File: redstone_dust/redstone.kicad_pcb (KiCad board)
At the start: 2 copper layers, 40 x 40 mm, 76 parts, among them J1 1x4_Pogo, J2 1x4_Pogo, J3 1x4_Pogo, J4 1x4_Pogo, J5 1x4_Pogo, J6 1x4_Pogo, J7 1x4_Pogo, J8 1x4_Pogo, J9 2.54mm_ProgrammingPin, Q1 BC108, Q2 BC108, Q3 BC108, Q4 BC108, SW1 SW_Push_Open, U1 RP2040, U3 TPS62162DSG

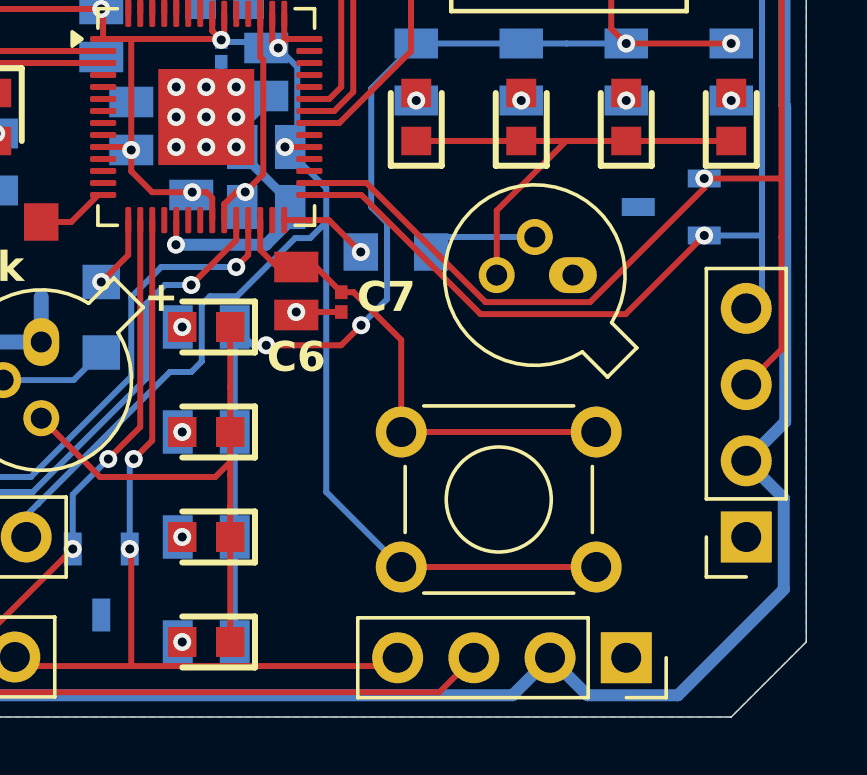
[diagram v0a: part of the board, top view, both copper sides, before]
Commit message: add dip switch to schematic, todo update pcb design
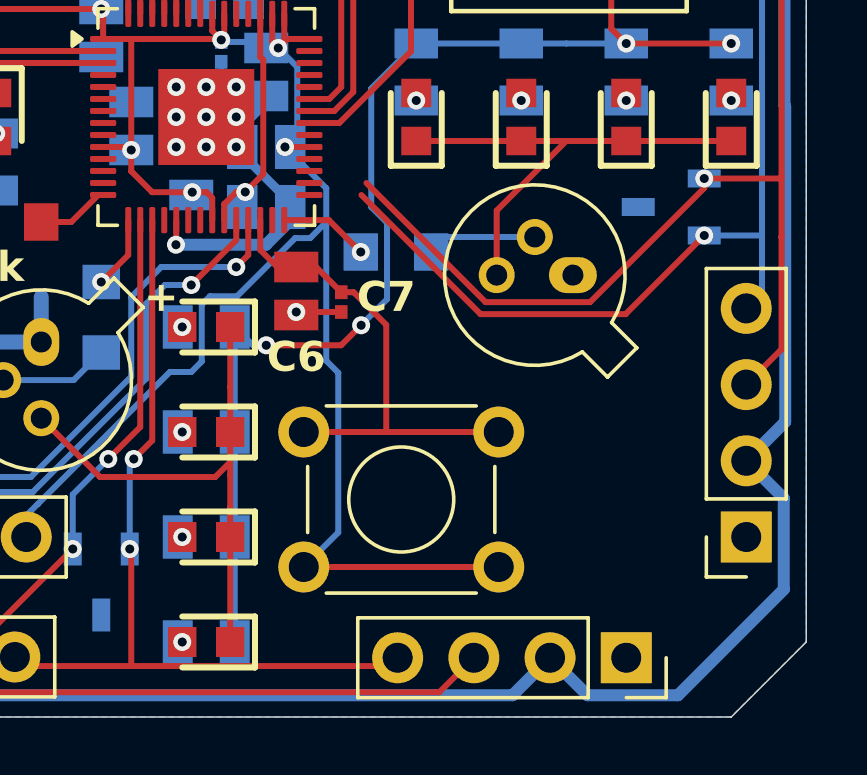
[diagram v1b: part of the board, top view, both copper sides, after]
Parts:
- moved SW1 3.25 mm to (144.8, 70.0)
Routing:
- net /E_TX: track 38.2 -> 36.3 mm
- net /E_RX: track 31.0 -> 29.3 mm
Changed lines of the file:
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@@
 	(net 66 "unconnected-(U1-GPIO4-Pad6)")
 	(net 67 "unconnected-(U1-GPIO5-Pad7)")
-	(net 68 "unconnected-(U1-GPIO20-Pad31)")
-	(net 69 "unconnected-(U1-GPIO21-Pad32)")
-	(net 70 "Net-(U1-GPIO12)")
-	(net 71 "unconnected-(U1-GPIO16-Pad27)")
-	(net 72 "Net-(SW1-B)")
-	(net 73 "unconnected-(U1-GPIO9-Pad12)")
-	(net 74 "unconnected-(U1-GPIO8-Pad11)")
+	(net 68 "unconnected-(U1-GPIO21-Pad32)")
+	(net 69 "Net-(U1-GPIO12)")
+	(net 70 "unconnected-(U1-GPIO16-Pad27)")
+	(net 71 "Net-(SW1-B)")
+	(net 72 "unconnected-(U1-GPIO9-Pad12)")
+	(net 73 "unconnected-(U1-GPIO8-Pad11)")
+	(net 74 "unconnected-(U1-GPIO20-Pad31)")
 	(footprint "SamacSys_Parts:LEDC1608X115N"
 		(layer "F.Cu")
@@
 	(footprint "Button_Switch_THT:SW_TH_Tactile_Omron_B3F-100x"
 		(layer "F.Cu")
-		(at 148 70 180)
+		(at 144.75 70 180)
 		(descr "Tactile switch, 6x6 mm, H4.3 mm, 6.5 mm pitch, https://omronfs.omron.com/en_US/ecb/products/pdf/en-b3f.pdf")
 		(tags "Omron B3F-10xx SPST 1P1T")
@@
 			(layers "*.Cu" "*.Mask")
 			(remove_unused_layers no)
-			(net 72 "Net-(SW1-B)")
+			(net 71 "Net-(SW1-B)")
 			(pinfunction "B")
 			(pintype "passive")
@@
 			(layers "*.Cu" "*.Mask")
 			(remove_unused_layers no)
-			(net 72 "Net-(SW1-B)")
+			(net 71 "Net-(SW1-B)")
 			(pinfunction "B")
 			(pintype "passive")
@@
 			(size 0.42 0.46)
 			(layers "F.Cu" "F.Mask" "F.Paste")
-			(net 72 "Net-(SW1-B)")
+			(net 71 "Net-(SW1-B)")
 			(pinfunction "1")
 			(pintype "passive")
@@
 			(layers "F.Cu" "F.Mask" "F.Paste")
 			(roundrect_rratio 0.25)
-			(net 74 "unconnected-(U1-GPIO8-Pad11)")
+			(net 73 "unconnected-(U1-GPIO8-Pad11)")
 			(pinfunction "GPIO8")
 			(pintype "bidirectional+no_connect")
@@
 			(layers "F.Cu" "F.Mask" "F.Paste")
 			(roundrect_rratio 0.25)
-			(net 73 "unconnected-(U1-GPIO9-Pad12)")
+			(net 72 "unconnected-(U1-GPIO9-Pad12)")
 			(pinfunction "GPIO9")
 			(pintype "bidirectional+no_connect")
@@
 			(layers "F.Cu" "F.Mask" "F.Paste")
 			(roundrect_rratio 0.25)
-			(net 70 "Net-(U1-GPIO12)")
+			(net 69 "Net-(U1-GPIO12)")
 			(pinfunction "GPIO12")
 			(pintype "bidirectional")
@@
 			(layers "F.Cu" "F.Mask" "F.Paste")
 			(roundrect_rratio 0.25)
-			(net 72 "Net-(SW1-B)")
+			(net 71 "Net-(SW1-B)")
 			(pinfunction "RUN")
 			(pintype "input")
@@
 			(layers "F.Cu" "F.Mask" "F.Paste")
 			(roundrect_rratio 0.25)
-			(net 71 "unconnected-(U1-GPIO16-Pad27)")
+			(net 70 "unconnected-(U1-GPIO16-Pad27)")
 			(pinfunction "GPIO16")
 			(pintype "bidirectional+no_connect")
@@
 			(layers "F.Cu" "F.Mask" "F.Paste")
 			(roundrect_rratio 0.25)
-			(net 68 "unconnected-(U1-GPIO20-Pad31)")
+			(net 74 "unconnected-(U1-GPIO20-Pad31)")
 			(pinfunction "GPIO20")
 			(pintype "bidirectional+no_connect")
@@
 			(layers "F.Cu" "F.Mask" "F.Paste")
 			(roundrect_rratio 0.25)
-			(net 69 "unconnected-(U1-GPIO21-Pad32)")
+			(net 68 "unconnected-(U1-GPIO21-Pad32)")
 			(pinfunction "GPIO21")
 			(pintype "bidirectional+no_connect")
@@
 			(size 1.02 1.47)
 			(layers "F.Cu" "F.Mask" "F.Paste")
-			(net 72 "Net-(SW1-B)")
+			(net 71 "Net-(SW1-B)")
 			(pinfunction "1")
 			(pintype "passive")
@@
 			(size 1.15 1.25)
 			(layers "B.Cu" "B.Mask" "B.Paste")
-			(net 70 "Net-(U1-GPIO12)")
+			(net 69 "Net-(U1-GPIO12)")
 			(pintype "passive")
 		)
@@
 	)
 	(segment
-		(start 141.5 70)
-		(end 148 70)
+		(start 138.25 70)
+		(end 144.75 70)
 		(width 0.2)
 		(layer "F.Cu")
@@
 	)
 	(segment
-		(start 139 58.5)
-		(end 139 67.5)
-		(width 0.2)
-		(layer "B.Cu")
-		(net 3)
-	)
-	(segment
 		(start 135.5 52.5)
 		(end 136.8 52.5)
@@
 	)
 	(segment
+		(start 139.401 68.849)
+		(end 138.25 70)
+		(width 0.2)
+		(layer "B.Cu")
+		(net 3)
+	)
+	(segment
 		(start 129 68.284785)
 		(end 129 69)
@@
 	)
 	(segment
-		(start 139 67.5)
-		(end 141.5 70)
+		(start 138.036 55.588832)
+		(end 138.036 53.336)
 		(width 0.2)
 		(layer "B.Cu")
@@
 	)
 	(segment
-		(start 138.036 55.588832)
-		(end 138.036 53.336)
+		(start 134.5 63.5)
+		(end 133.7862 63.5)
 		(width 0.2)
 		(layer "B.Cu")
@@
 	)
 	(segment
-		(start 134.5 63.5)
-		(end 133.7862 63.5)
+		(start 139 58.5)
+		(end 139 63.12224)
 		(width 0.2)
 		(layer "B.Cu")
@@
 	)
 	(segment
+		(start 139.401 63.52324)
+		(end 139.401 68.849)
+		(width 0.2)
+		(layer "B.Cu")
+		(net 3)
+	)
+	(segment
 		(start 139 58.5)
 		(end 138.464 59.036)
@@
 	)
 	(segment
+		(start 139 63.12224)
+		(end 139.401 63.52324)
+		(width 0.2)
+		(layer "B.Cu")
+		(net 3)
+	)
+	(segment
 		(start 129.383785 67.901)
 		(end 129 68.284785)
@@
 	)
 	(segment
-		(start 151.6 57.366167)
-		(end 151.6 57.05)
+		(start 147.795167 61.171)
+		(end 151.6 57.366167)
 		(width 0.2)
 		(layer "F.Cu")
@@
 	)
 	(segment
-		(start 154.176 47.231)
-		(end 154.176 57)
-		(width 0.2)
-		(layer "F.Cu")
-		(net 28)
-	)
-	(segment
-		(start 154.176 57)
-		(end 154.176 58.998765)
-		(width 0.2)
-		(layer "F.Cu")
-		(net 28)
-	)
-	(segment
 		(start 140.337753 57.199999)
 		(end 144.308754 61.171)
@@
 	)
 	(segment
-		(start 147.795167 61.171)
-		(end 151.6 57.366167)
+		(start 154.176 47.231)
+		(end 154.176 57)
 		(width 0.2)
 		(layer "F.Cu")
@@
 	)
 	(segment
-		(start 138.4375 57.199999)
-		(end 140.337753 57.199999)
+		(start 154.176 57)
+		(end 154.176 58.998765)
 		(width 0.2)
 		(layer "F.Cu")
@@
 	)
 	(segment
+		(start 151.6 57.366167)
+		(end 151.6 57.05)
+		(width 0.2)
+		(layer "F.Cu")
+		(net 28)
+	)
+	(segment
 		(start 154.176 58.998765)
 		(end 154.174765 59)
@@
 	)
 	(segment
-		(start 138.4375 57.6)
-		(end 140.170654 57.6)
-		(width 0.2)
-		(layer "F.Cu")
-		(net 29)
-	)
-	(segment
 		(start 148.978 61.572)
 		(end 151.6 58.95)
@@
 		(width 0.2)
 		(layer "F.Cu")
-		(net 70)
+		(net 69)
 	)
 	(segment
@@
 		(width 0.2)
 		(layer "F.Cu")
-		(net 70)
+		(net 69)
 	)
 	(via
@@
 		(drill 0.3)
 		(layers "F.Cu" "B.Cu")
-		(net 70)
+		(net 69)
 	)
 	(segment
-		(start 141.5 65.5)
-		(end 148 65.5)
+		(start 138.25 65.5)
+		(end 141 65.5)
 		(width 0.2)
 		(layer "F.Cu")
-		(net 72)
+		(net 71)
 	)
 	(segment
@@
 		(width 0.2)
 		(layer "F.Cu")
-		(net 72)
+		(net 71)
 	)
 	(segment
-		(start 136.8 59.4329)
-		(end 137.3671 60)
+		(start 141 65.5)
+		(end 144.75 65.5)
 		(width 0.2)
 		(layer "F.Cu")
-		(net 72)
+		(net 71)
 	)
 	(segment
-		(start 136.8 58.4375)
-		(end 136.8 59.4329)
+		(start 141 61.928584)
+		(end 141 65.5)
 		(width 0.2)
 		(layer "F.Cu")
-		(net 72)
+		(net 71)
 	)
 	(segment
-		(start 139.91 60.84)
-		(end 139.5 60.84)
+		(start 139.5 60.84)
+		(end 139.911416 60.84)
 		(width 0.2)
 		(layer "F.Cu")
-		(net 72)
+		(net 71)
 	)
 	(segment
-		(start 138 60)
-		(end 138.66 60)
+		(start 136.8 59.4329)
+		(end 137.3671 60)
+		(width 0.2)
+		(layer "F.Cu")
+		(net 71)
+	)
+	(segment
+		(start 136.8 58.4375)
+		(end 136.8 59.4329)
 		(width 0.2)
 		(layer "F.Cu")
-		(net 72)
+		(net 71)
 	)
 	(segment
-		(start 141.5 65.5)
-		(end 141.5 62.43)
+		(start 138 60)
+		(end 138.66 60)
 		(width 0.2)
 		(layer "F.Cu")
-		(net 72)
+		(net 71)
 	)
 	(segment
-		(start 141.5 62.43)
-		(end 139.91 60.84)
+		(start 139.911416 60.84)
+		(end 141 61.928584)
 		(width 0.2)
 		(layer "F.Cu")
-		(net 72)
+		(net 71)
 	)
 	(segment
@@
 		(width 0.2)
 		(layer "F.Cu")
-		(net 72)
+		(net 71)
 	)
 	(zone

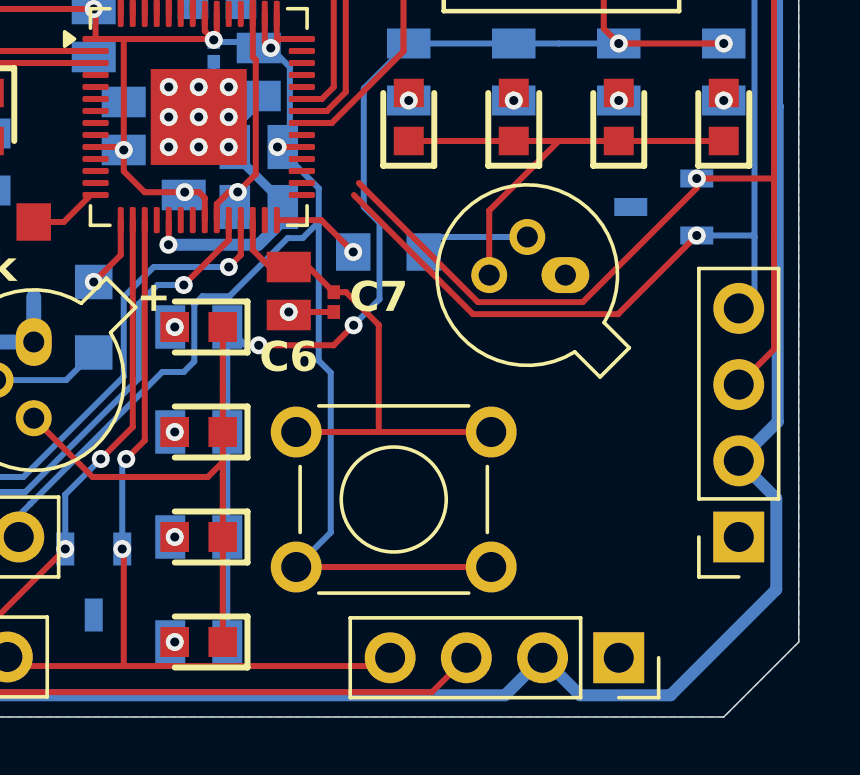
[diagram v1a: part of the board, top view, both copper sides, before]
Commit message: remove dip switch, cannot find one that fits in board space
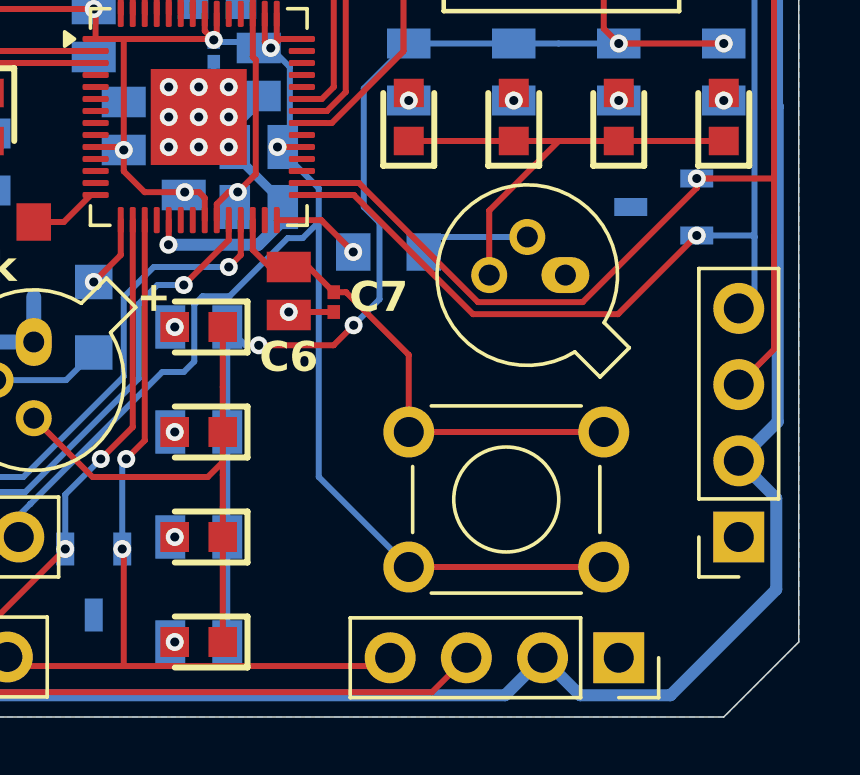
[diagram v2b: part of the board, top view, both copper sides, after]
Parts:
- moved SW1 3.75 mm to (148.5, 70.0)
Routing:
- net /E_TX: track 36.3 -> 38.2 mm
- net /E_RX: track 29.3 -> 31.0 mm
- net /3.3V_LOCAL: track 103.6 -> 104.2 mm
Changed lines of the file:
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@@
 	(footprint "Button_Switch_THT:SW_TH_Tactile_Omron_B3F-100x"
 		(layer "F.Cu")
-		(at 144.75 70 180)
+		(at 148.5 70 180)
 		(descr "Tactile switch, 6x6 mm, H4.3 mm, 6.5 mm pitch, https://omronfs.omron.com/en_US/ecb/products/pdf/en-b3f.pdf")
 		(tags "Omron B3F-10xx SPST 1P1T")
@@
 	)
 	(segment
+		(start 142 70)
+		(end 148.5 70)
+		(width 0.2)
+		(layer "F.Cu")
+		(net 3)
+	)
+	(segment
 		(start 132.5 56.81)
 		(end 133.196166 57.506166)
@@
 	)
 	(segment
-		(start 138.25 70)
-		(end 144.75 70)
-		(width 0.2)
-		(layer "F.Cu")
-		(net 3)
-	)
-	(segment
 		(start 135.2 52.129998)
 		(end 135.5 52.429998)
@@
 	)
 	(segment
+		(start 139 58.5)
+		(end 139 67)
+		(width 0.2)
+		(layer "B.Cu")
+		(net 3)
+	)
+	(segment
 		(start 135.5 52.5)
 		(end 136.8 52.5)
@@
 	)
 	(segment
-		(start 139.401 68.849)
-		(end 138.25 70)
-		(width 0.2)
-		(layer "B.Cu")
-		(net 3)
-	)
-	(segment
 		(start 129 68.284785)
 		(end 129 69)
@@
 	)
 	(segment
-		(start 139 58.5)
-		(end 139 63.12224)
-		(width 0.2)
-		(layer "B.Cu")
-		(net 3)
-	)
-	(segment
 		(start 137.964 59.036)
 		(end 136.026 60.974)
@@
 	)
 	(segment
-		(start 139.401 63.52324)
-		(end 139.401 68.849)
+		(start 139 58.5)
+		(end 138.464 59.036)
 		(width 0.2)
 		(layer "B.Cu")
@@
 	)
 	(segment
-		(start 139 58.5)
-		(end 138.464 59.036)
+		(start 139 67)
+		(end 142 70)
 		(width 0.2)
 		(layer "B.Cu")
@@
 	)
 	(segment
-		(start 139 63.12224)
-		(end 139.401 63.52324)
-		(width 0.2)
-		(layer "B.Cu")
-		(net 3)
-	)
-	(segment
 		(start 129.383785 67.901)
 		(end 129 68.284785)
@@
 	)
 	(segment
+		(start 140.337753 57.199999)
+		(end 138.4375 57.199999)
+		(width 0.2)
+		(layer "F.Cu")
+		(net 28)
+	)
+	(segment
 		(start 154.176 59)
 		(end 154.176 62.744)
@@
 		(net 29)
 	)
+	(segment
+		(start 140.170654 57.6)
+		(end 138.4375 57.6)
+		(width 0.2)
+		(layer "F.Cu")
+		(net 29)
+	)
 	(via
 		(at 151.6 58.95)
@@
 	)
 	(segment
-		(start 138.25 65.5)
-		(end 141 65.5)
-		(width 0.2)
-		(layer "F.Cu")
-		(net 71)
-	)
-	(segment
 		(start 137.3671 60)
 		(end 138 60)
@@
 	)
 	(segment
-		(start 141 65.5)
-		(end 144.75 65.5)
+		(start 139.5 60.84)
+		(end 139.911416 60.84)
 		(width 0.2)
 		(layer "F.Cu")
@@
 	)
 	(segment
-		(start 141 61.928584)
-		(end 141 65.5)
+		(start 142 65.5)
+		(end 142 62.928584)
 		(width 0.2)
 		(layer "F.Cu")
@@
 	)
 	(segment
-		(start 139.5 60.84)
-		(end 139.911416 60.84)
+		(start 136.8 59.4329)
+		(end 137.3671 60)
 		(width 0.2)
 		(layer "F.Cu")
@@
 	)
 	(segment
-		(start 136.8 59.4329)
-		(end 137.3671 60)
+		(start 136.8 58.4375)
+		(end 136.8 59.4329)
 		(width 0.2)
 		(layer "F.Cu")
@@
 	)
 	(segment
-		(start 136.8 58.4375)
-		(end 136.8 59.4329)
+		(start 142 62.928584)
+		(end 139.911416 60.84)
 		(width 0.2)
 		(layer "F.Cu")
@@
 	)
 	(segment
-		(start 139.911416 60.84)
-		(end 141 61.928584)
+		(start 142 65.5)
+		(end 148.5 65.5)
 		(width 0.2)
 		(layer "F.Cu")

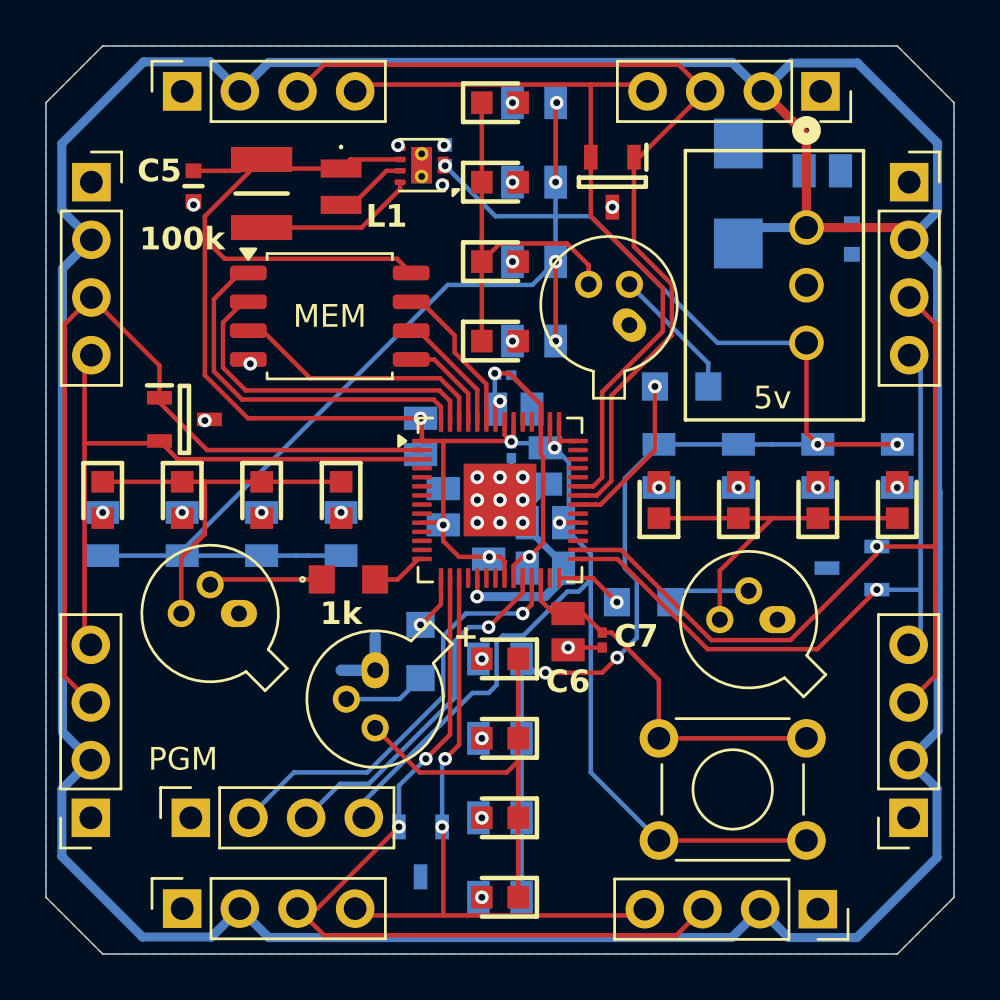
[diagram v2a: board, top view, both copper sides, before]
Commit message: switch redstone dust transistor to a much smaller one, todo switch transistors on other tiles as well
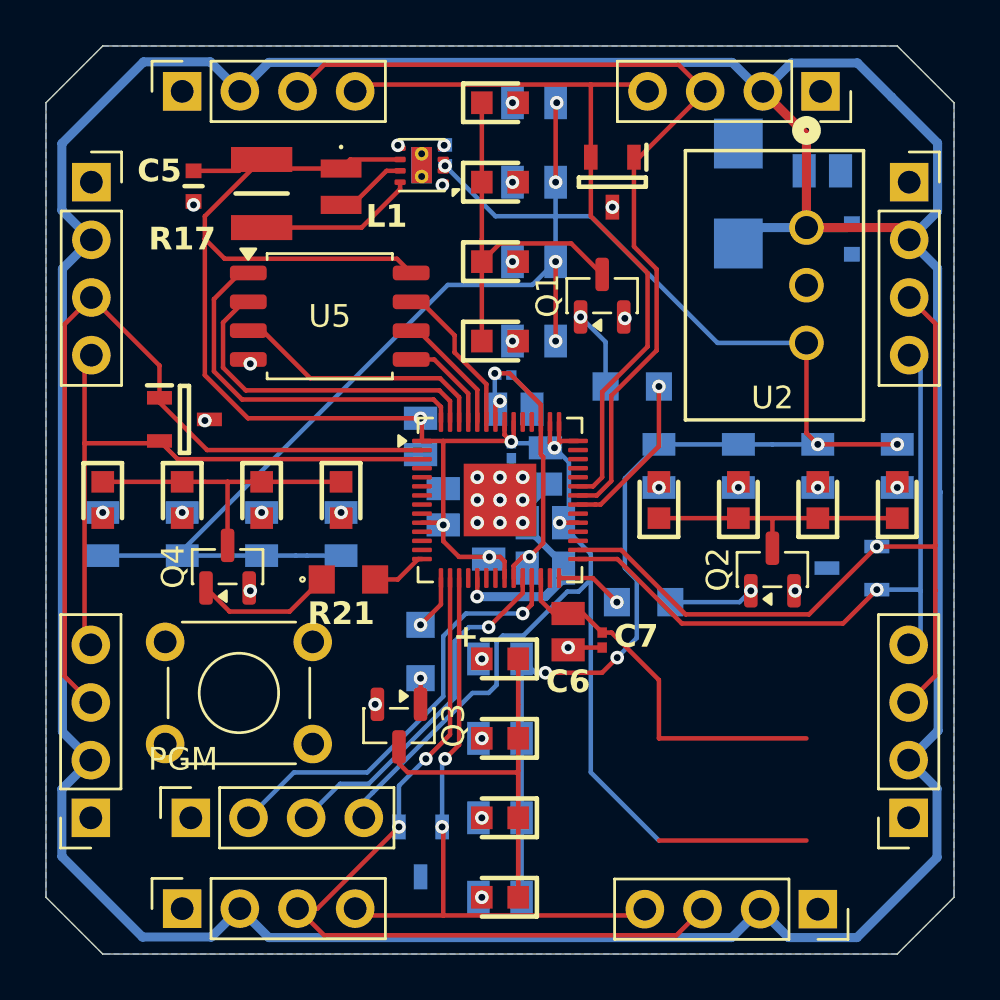
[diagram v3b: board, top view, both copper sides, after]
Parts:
- Q1, Q2, Q3, Q4: value BC108 -> MMBT3904; footprint Package_TO_SOT_THT:TO-18-3 -> Package_TO_SOT_SMD:SOT-23
- moved SW1 22.2 mm to (126.8, 65.8)
- moved Q3 2.65 mm to (130.6, 64.9)
- moved Q2 2.22 mm to (147.0, 58.1), turned to 90 degrees
- moved R18 2.18 mm to (140.8, 50.0), turned to 0 degrees
- moved Q4 2.12 mm to (123.0, 57.9), turned to 90 degrees
- moved Q1 1.77 mm to (139.5, 46.0), turned to 90 degrees
- renumbered 200 to R1, 200 to R11, 200 to R15, 100k to R17, 1k to R18, 1k to R19, 1k to R20, 1k to R21, 200 to R6, 5v to U2, MEM to U5
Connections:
- Q1 pad 1: GND -> Net-(Q1-B)
- Q1 pad 2: Net-(Q1-B) -> GND
- Q2 pad 1: GND -> Net-(Q2-B)
- Q2 pad 2: Net-(Q2-B) -> GND
- Q3 pad 1: GND -> Net-(Q3-B)
- Q3 pad 2: Net-(Q3-B) -> GND
- Q4 pad 1: GND -> Net-(Q4-B)
- Q4 pad 2: Net-(Q4-B) -> GND
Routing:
- net Net-(D5-K): track 15.9 -> 11.8 mm
- net Net-(D13-K): track 16.7 -> 13.3 mm
- net GND: track 19.3 -> 16.7 mm, vias 18 -> 22
- net Net-(Q3-B): track 3.65 -> 1.15 mm, vias 0 -> 1
- net Net-(Q1-B): track 5.94 -> 3.63 mm, vias 0 -> 1
- net Net-(D10-K): track 17.8 -> 16.7 mm
- net /E_TX: track 38.2 -> 37.0 mm
- net Net-(Q4-B): track 5.02 -> 6.12 mm
- net /E_RX: track 31.0 -> 30.1 mm
- net /N_TX: track 41.1 -> 40.5 mm
- net /N_RX: track 34.1 -> 33.5 mm
- net Net-(Q2-B): track 3.66 -> 3.76 mm, vias 0 -> 1
